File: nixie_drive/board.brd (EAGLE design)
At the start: 150 x 100 mm, 53 parts, among them IC1 74141N, IC2 74HC138D, IC3 74HC138D, U1 ATMEGA328P-AU

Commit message: [fix] hole
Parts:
- moved RESET 4.61 mm to (5.92, 89.1)
- moved U$2 2.00 mm to (8.65, 82.7)
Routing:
- net GND: track 272.5 -> 265.5 mm
- net +5V: track 308.9 -> 305.8 mm
- net N$15: track 22.9 -> 23.9 mm
- net N$2: track 9.86 -> 10.6 mm

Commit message: [add] 面付け
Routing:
- net RHDP: track 120.7 -> 149.6 mm
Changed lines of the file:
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@@
 <setting verticaltext="up"/>
 </settings>
-<grid distance="1" unitdist="mm" unit="mm" style="lines" multiple="1" display="yes" altdistance="0.5" altunitdist="mm" altunit="mm"/>
+<grid distance="39.3700787" unitdist="mil" unit="mil" style="lines" multiple="1" display="yes" altdistance="0.5" altunitdist="mm" altunit="mm"/>
 <layers>
 <layer number="1" name="Top" color="4" fill="1" visible="yes" active="yes"/>
@@
 <contactref element="U$6" pad="P$8"/>
 <contactref element="U1" pad="32"/>
-<wire x1="13.6144" y1="89.6112" x2="13.6144" y2="87.5792" width="0.254" layer="1"/>
-<wire x1="17.6784" y1="93.6752" x2="13.6144" y2="89.6112" width="0.254" layer="1"/>
-<wire x1="17.6784" y1="98.9584" x2="17.6784" y2="93.6752" width="0.254" layer="1"/>
-<wire x1="18.288" y1="99.568" x2="17.6784" y2="98.9584" width="0.254" layer="1"/>
-<wire x1="109.728" y1="99.568" x2="18.288" y2="99.568" width="0.254" layer="1"/>
-<wire x1="113.3856" y1="95.9104" x2="109.728" y2="99.568" width="0.254" layer="1"/>
-<wire x1="120.2944" y1="89.0016" x2="113.3856" y2="95.9104" width="0.254" layer="16"/>
-<wire x1="13.6144" y1="87.5792" x2="13.446" y2="87.4118" width="0.254" layer="1"/>
-<wire x1="120.2944" y1="89.0016" x2="120.33" y2="88.9" width="0.254" layer="16"/>
-<via x="113.3856" y="95.9104" extent="1-16" drill="0.3048"/>
+<wire x1="13.446" y1="87.4118" x2="13.446" y2="88.446" width="0.254" layer="1"/>
+<wire x1="13.446" y1="88.446" x2="17" y2="92" width="0.254" layer="1"/>
+<via x="17" y="92" extent="1-16" drill="0.35"/>
+<wire x1="135.20408125" y1="88.0166" x2="135.93591875" y2="88.0166" width="0.254" layer="16"/>
+<wire x1="135.93591875" y1="88.0166" x2="136.4534" y2="88.53408125" width="0.254" layer="16"/>
+<wire x1="136.4534" y1="88.53408125" x2="136.4534" y2="89.26591875" width="0.254" layer="16"/>
+<wire x1="132.59348125" y1="90.6272" x2="135.20408125" y2="88.0166" width="0.254" layer="16"/>
+<wire x1="68.5132625" y1="96.9264" x2="63.5868625" y2="92" width="0.254" layer="16"/>
+<wire x1="63.5868625" y1="92" x2="17" y2="92" width="0.254" layer="16"/>
+<wire x1="136.4534" y1="89.26591875" x2="128.79291875" y2="96.9264" width="0.254" layer="16"/>
+<wire x1="128.79291875" y1="96.9264" x2="68.5132625" y2="96.9264" width="0.254" layer="16"/>
+<wire x1="120.33" y1="88.9" x2="122.0572" y2="90.6272" width="0.254" layer="16"/>
+<wire x1="122.0572" y1="90.6272" x2="132.59348125" y2="90.6272" width="0.254" layer="16"/>
 </signal>
 <signal name="N$15">

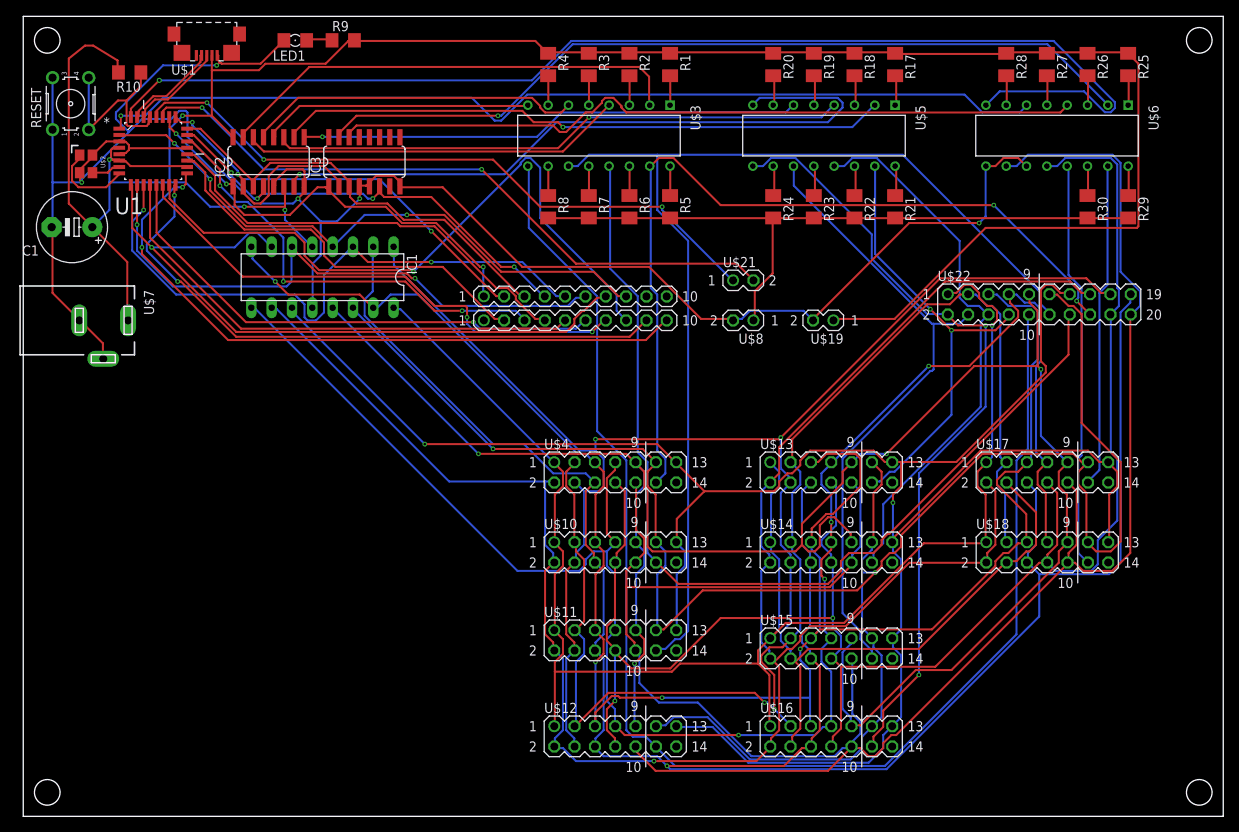
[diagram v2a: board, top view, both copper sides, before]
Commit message: [fix] 太さ・ガーバー出力(FusionPCB)
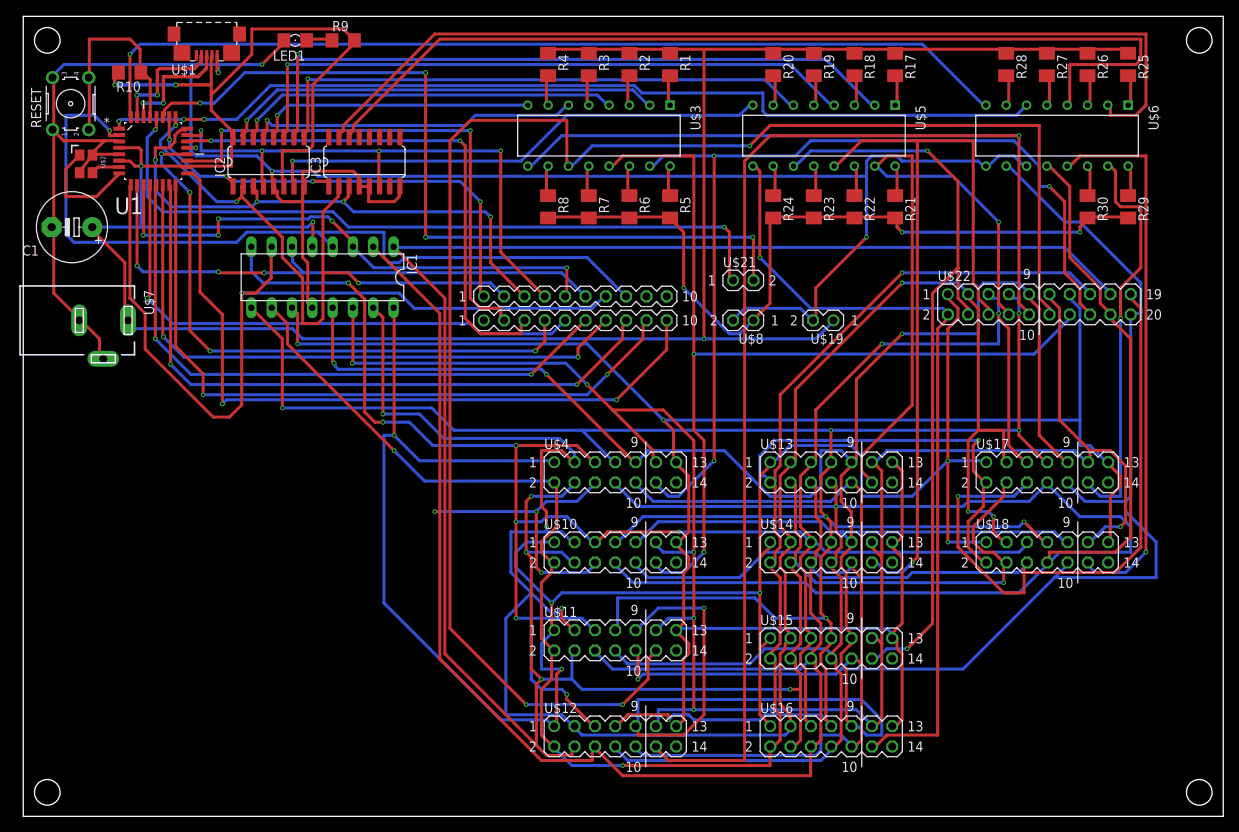
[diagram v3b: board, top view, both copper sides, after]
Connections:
- net NIXIE1: now also IC1.15
- net NIXIE2: no longer IC1.15
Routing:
- net NIXIE8: track 244.0 -> 331.5 mm, vias 2 -> 5
- net DOT0: track 214.3 -> 299.3 mm, vias 2 -> 1
- net NIXIE1: track 170.1 -> 252.3 mm, vias 2 -> 6
- net NIXIE4: track 248.8 -> 318.9 mm
- net NIXIE3: track 229.1 -> 295.2 mm, vias 4 -> 8
- net NIXIE_ANODE3: track 136.3 -> 201.6 mm, vias 0 -> 3
- net NIXIE0: track 196.5 -> 257.0 mm, vias 1 -> 6
- net NIXIE9: track 265.1 -> 323.6 mm, vias 1 -> 4
- net +5V: track 305.8 -> 354.2 mm, vias 4 -> 5
- net NIXIE2: track 239.7 -> 279.6 mm, vias 4 -> 9
- net NIXIE_ANODE4: track 173.8 -> 208.3 mm, vias 0 -> 1
- net NIXIE_ANODE6: track 69.0 -> 100.3 mm, vias 0 -> 1
- net RHDP: track 149.6 -> 118.5 mm
- net ANODE9: track 94.2 -> 121.7 mm
- net N$6: track 75.8 -> 102.2 mm, vias 3 -> 1
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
